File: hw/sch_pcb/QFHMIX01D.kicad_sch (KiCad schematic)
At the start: 81 parts, among them J1 HEADER_1x08, J2 +9V, M1 HOLE, M2 HOLE, M3 HOLE, M4 HOLE, M5 HOLE, M6 HOLE, M7 HOLE, M8 HOLE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

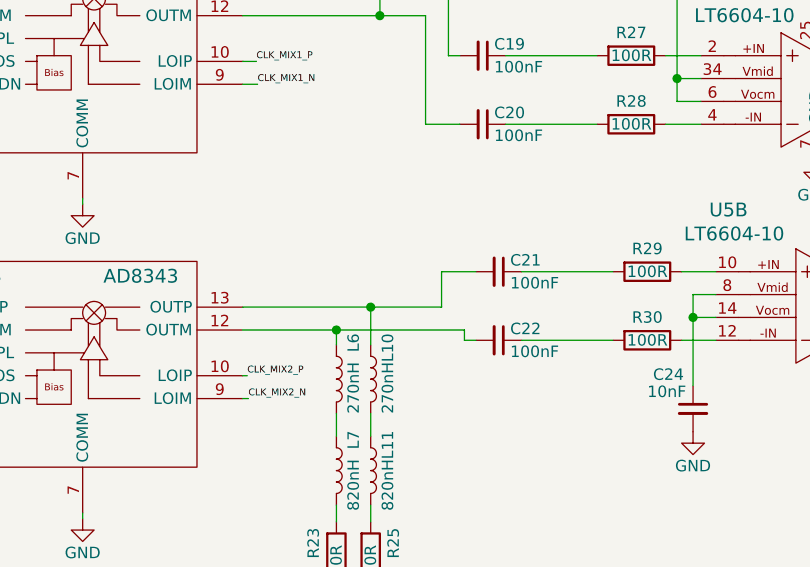
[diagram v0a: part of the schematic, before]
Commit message: Add notes to measured values.
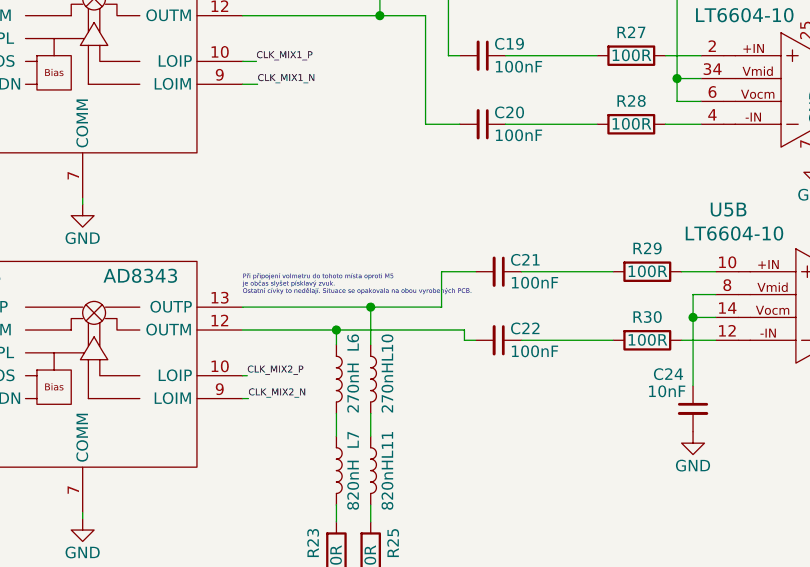
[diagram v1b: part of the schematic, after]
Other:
- note added: "Při připojení volmetru do tohoto místa oproti M5 je občas slyšet písklavý zvuk. Ostatní cívky to nedělají. Situace se opakovala na obou vyrobených PCB."
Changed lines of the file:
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@@
     (stroke (width 0) (type dash) (color 0 0 0 0))
+  )
+  (text "Při připojení volmetru do tohoto místa oproti M5\nje občas slyšet písklavý zvuk.\nOstatní cívky to nedělají. Situace se opakovala na obou vyrobených PCB.  "
+    (at 154.94 99.06 0)
+    (effects (font (size 0.508 0.508)) (justify left bottom))
   )
   (text "POWER INPUT" (at 238.76 38.1 0)
